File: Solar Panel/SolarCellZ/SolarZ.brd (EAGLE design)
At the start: 99 x 99 mm, 29 parts, among them X1 BU-SMA-V

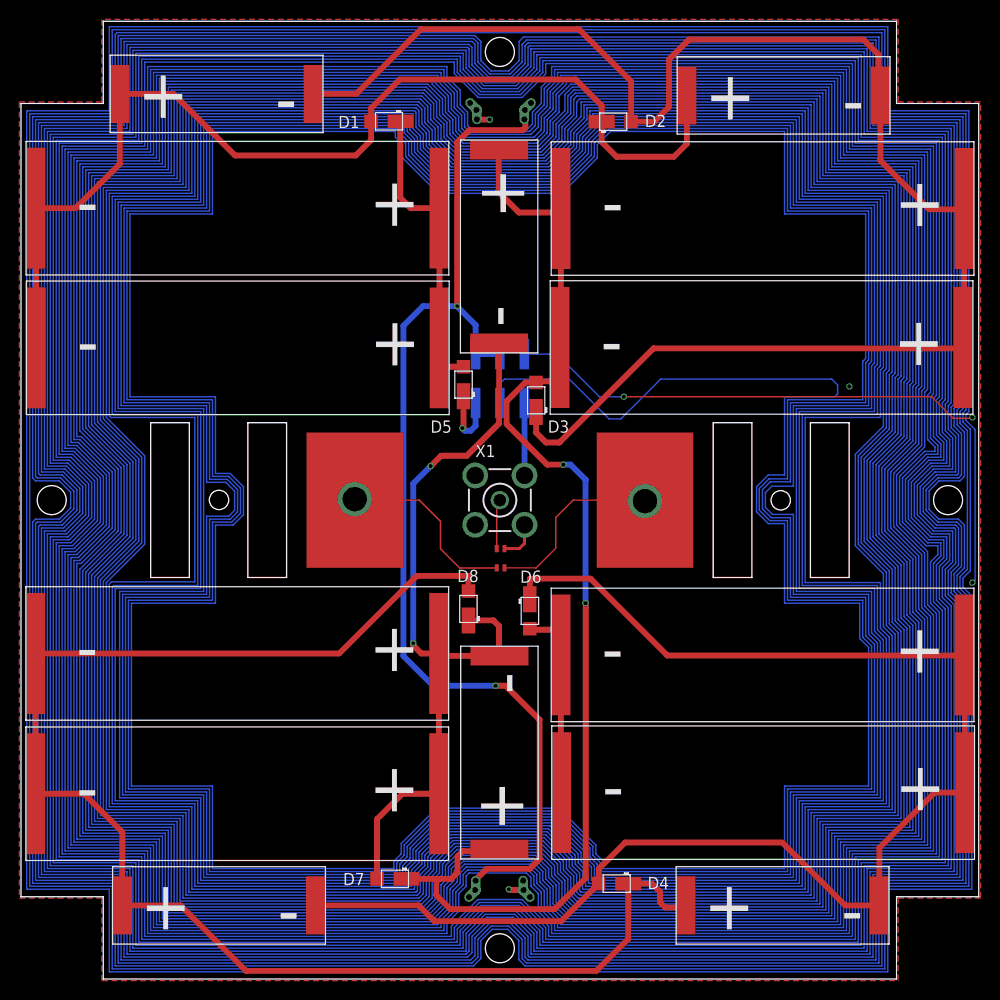
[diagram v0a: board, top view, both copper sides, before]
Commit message: Moved magnetorquers and shrunk outside of Z board
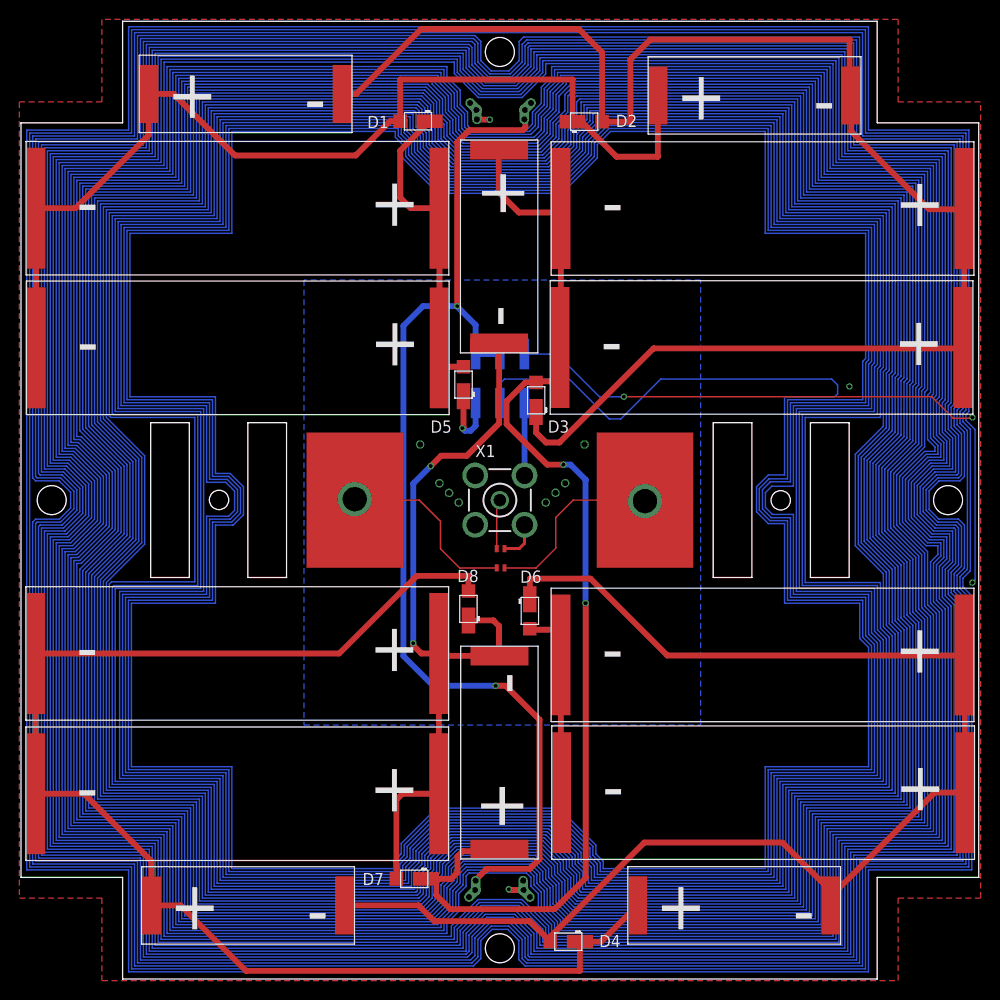
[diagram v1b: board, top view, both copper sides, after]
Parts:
- moved D4 7.81 mm to (52.3, -0.39)
- moved 6 5.00 mm to (80.5, 7.36)
- moved 1 3.00 mm to (30.0, 91.2)
- moved 13 3.00 mm to (82.6, 91.1)
- moved 7 3.00 mm to (30.2, 7.36)
- moved D1 3.00 mm to (36.8, 84.4)
- moved D2 3.00 mm to (54.0, 84.4)
- moved D7 2.00 mm to (36.4, 6.10)
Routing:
- net N8: track 152.2 -> 141.2 mm
- net N$11: track 147.7 -> 143.8 mm
- net N$6: track 109.8 -> 106.7 mm
- net N$12: track 121.0 -> 119.0 mm
- net N$7: track 31.2 -> 32.4 mm
- net N$10: track 161.6 -> 160.5 mm
- net N$9: track 80.5 -> 79.7 mm
- net GND: vias 2 -> 10
- added copper zone on layer 16, net GND
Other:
- outline, holes or cut-outs redrawn
